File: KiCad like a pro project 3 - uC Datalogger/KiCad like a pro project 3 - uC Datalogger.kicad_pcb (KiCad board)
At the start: 2 copper layers, 29 parts, among them J1 Conn_01x04_Male, J2 Conn_01x09_Male, J3 Conn_01x04_Male, J4 Conn_02x03_Odd_Even, U1 24LC1025, U2 24LC1025, U3 DS1337S+, U4 ATMEGA328P_VQFNVQFN, Y1 32.768 KHz, Y2 16 MHz

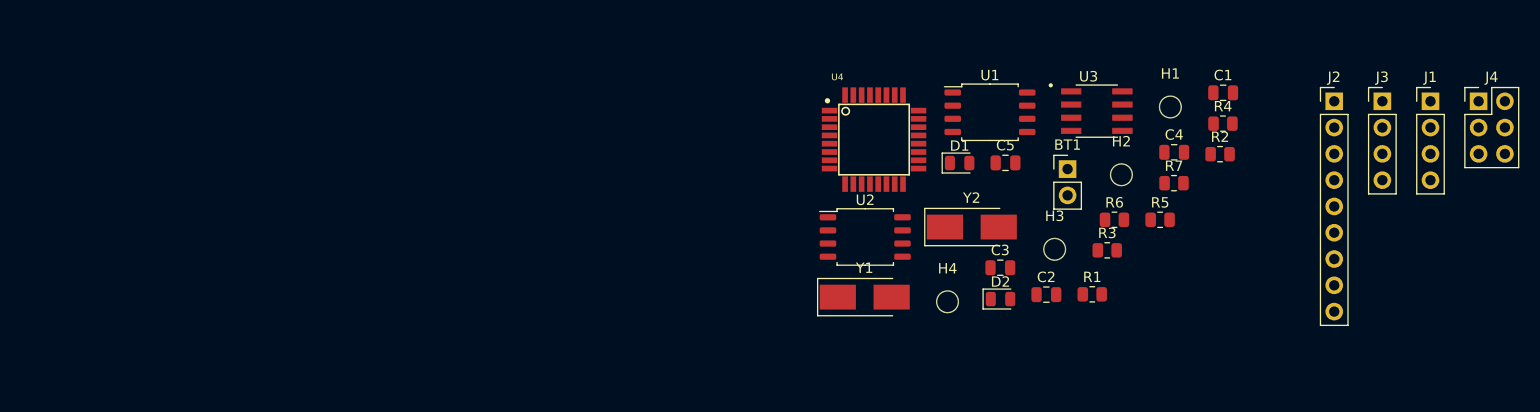
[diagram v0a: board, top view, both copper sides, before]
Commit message: completed placement of foodprints
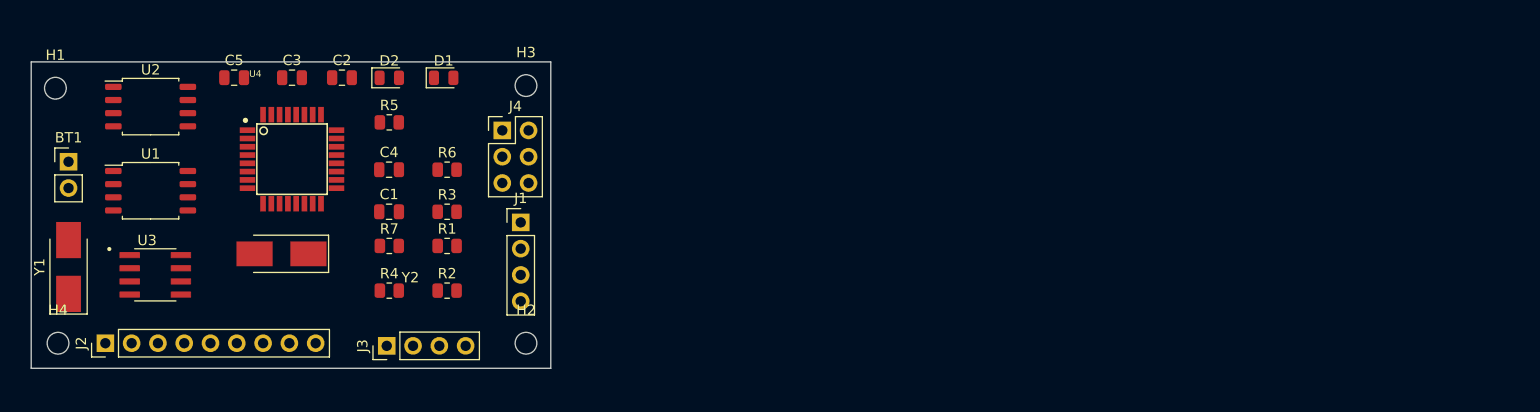
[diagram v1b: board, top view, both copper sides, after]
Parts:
- moved J2 121.0 mm to (54.9, 114.8), turned to 90 degrees
- moved H1 107.7 mm to (50.0, 90.2)
- moved J3 99.0 mm to (82.1, 115.1), turned to 90 degrees
- moved BT1 96.5 mm to (51.3, 97.3)
- moved J4 94.4 mm to (93.2, 94.2)
- moved U3 92.3 mm to (59.7, 108.2)
- moved J1 88.7 mm to (95.0, 103.1)
- moved H4 86.0 mm to (50.3, 114.8)
- moved R4 82.1 mm to (82.3, 109.7)
- moved U1 81.4 mm to (59.2, 100.1)
- moved C1 81.4 mm to (82.3, 102.1)
- moved Y1 77.0 mm to (51.3, 107.4), turned to 90 degrees
- moved R7 76.1 mm to (82.3, 105.4)
- moved C4 75.9 mm to (82.3, 98.0)
- moved R2 75.8 mm to (87.9, 109.7)
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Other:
- board outline added: 50.2 x 29.6 mm

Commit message: Started wiring
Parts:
- moved U3 0.56 mm to (59.1, 108.2)
- moved U1 0.31 mm to (58.9, 100.1)
- moved U2 0.31 mm to (58.9, 91.9)
- turned C1 to 180 degrees
- turned R4 to 180 degrees
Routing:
- net /Vcc: track 0.00 -> 127.1 mm, vias 0 -> 2
- net /SCL: track 0.00 -> 79.0 mm, vias 0 -> 4
- net Net-(BT1-Pad1): track 0.00 -> 52.9 mm, vias 0 -> 2
- net Net-(R2-Pad2): track 0.00 -> 50.3 mm
- net /TX: track 0.00 -> 43.2 mm, vias 0 -> 1
- net GND: track 0.00 -> 38.7 mm, vias 0 -> 3
- net /D2: track 0.00 -> 37.2 mm
- net /RX: track 0.00 -> 35.8 mm, vias 0 -> 1
- net Net-(R4-Pad2): track 0.00 -> 32.1 mm, vias 0 -> 2
- net /SDA: track 0.00 -> 28.7 mm, vias 0 -> 3
- net /D3: track 0.00 -> 27.7 mm
- net /MOSI: track 0.00 -> 26.9 mm, vias 0 -> 1
- net /MISO: track 0.00 -> 25.7 mm
- net /D4: track 0.00 -> 24.7 mm
- net /RESET: track 0.00 -> 22.8 mm, vias 0 -> 2
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- added copper zone on F.Cu, net GND

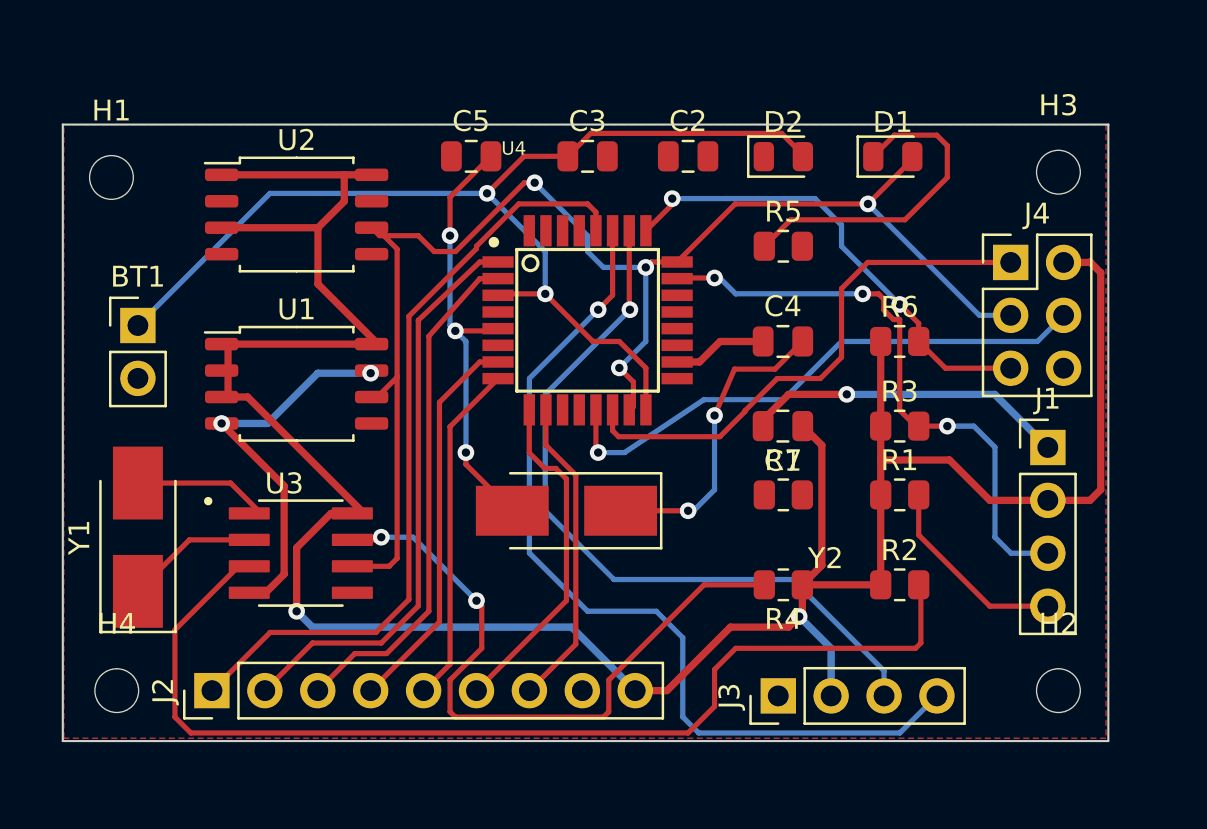
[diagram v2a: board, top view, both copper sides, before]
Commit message: Removed wires, redrawn pcb outline
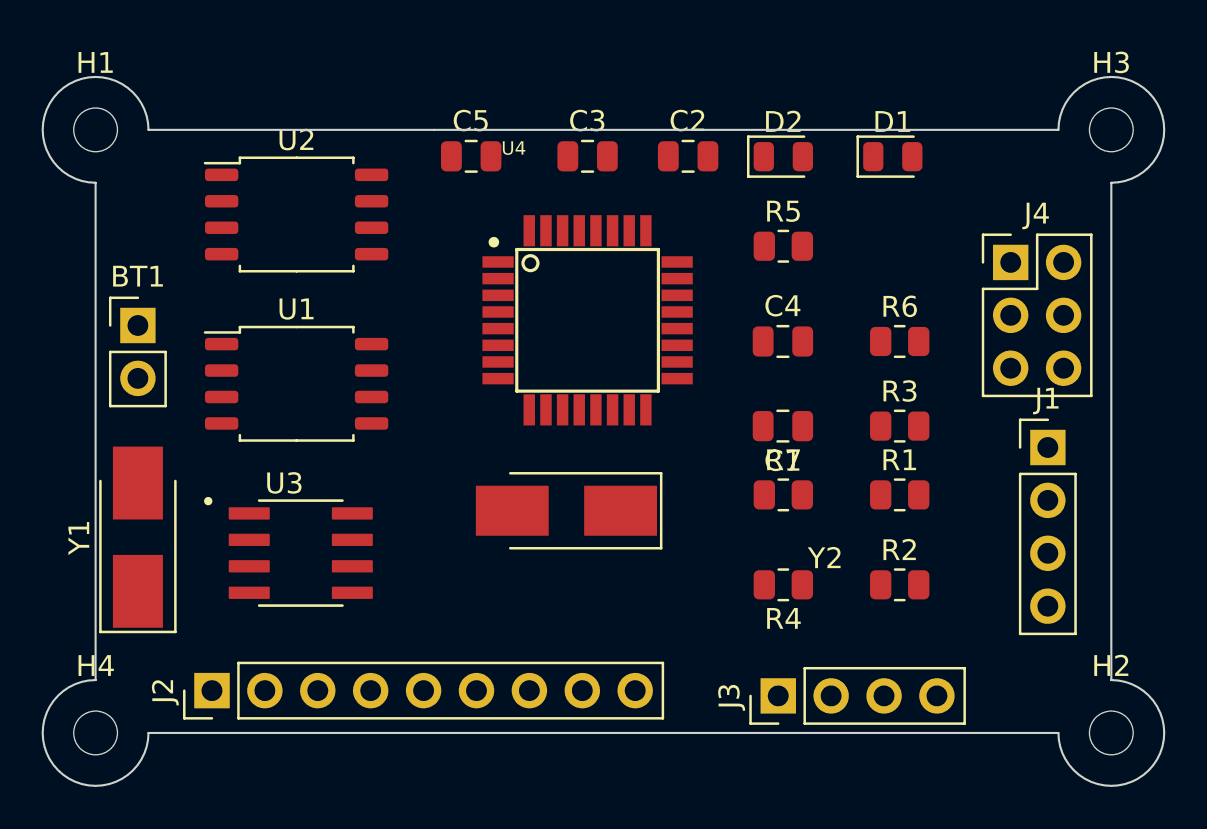
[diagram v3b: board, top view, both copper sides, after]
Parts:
- moved H2 3.25 mm to (98.0, 116.8)
- moved H3 3.25 mm to (98.0, 87.9)
- moved H1 2.41 mm to (49.3, 87.9)
- moved H4 2.27 mm to (49.3, 116.8)
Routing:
- net /Vcc: track 127.1 -> 0.00 mm, vias 2 -> 0
- net /SCL: track 79.0 -> 0.00 mm, vias 4 -> 0
- net Net-(BT1-Pad1): track 52.9 -> 0.00 mm, vias 2 -> 0
- net Net-(R2-Pad2): track 50.3 -> 0.00 mm
- net /TX: track 43.2 -> 0.00 mm, vias 1 -> 0
- net GND: track 38.7 -> 0.00 mm, vias 3 -> 0
- net /D2: track 37.2 -> 0.00 mm
- net /RX: track 35.8 -> 0.00 mm, vias 1 -> 0
- net Net-(R4-Pad2): track 32.1 -> 0.00 mm, vias 2 -> 0
- net /SDA: track 28.7 -> 0.00 mm, vias 3 -> 0
- net /D3: track 27.7 -> 0.00 mm
- net /MOSI: track 26.9 -> 0.00 mm, vias 1 -> 0
- net /MISO: track 25.7 -> 0.00 mm
- net /D4: track 24.7 -> 0.00 mm
- net /RESET: track 22.8 -> 0.00 mm, vias 2 -> 0
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- removed copper zone on F.Cu, net GND
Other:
- board size 50.2 x 29.6 mm -> 53.8 x 34 mm

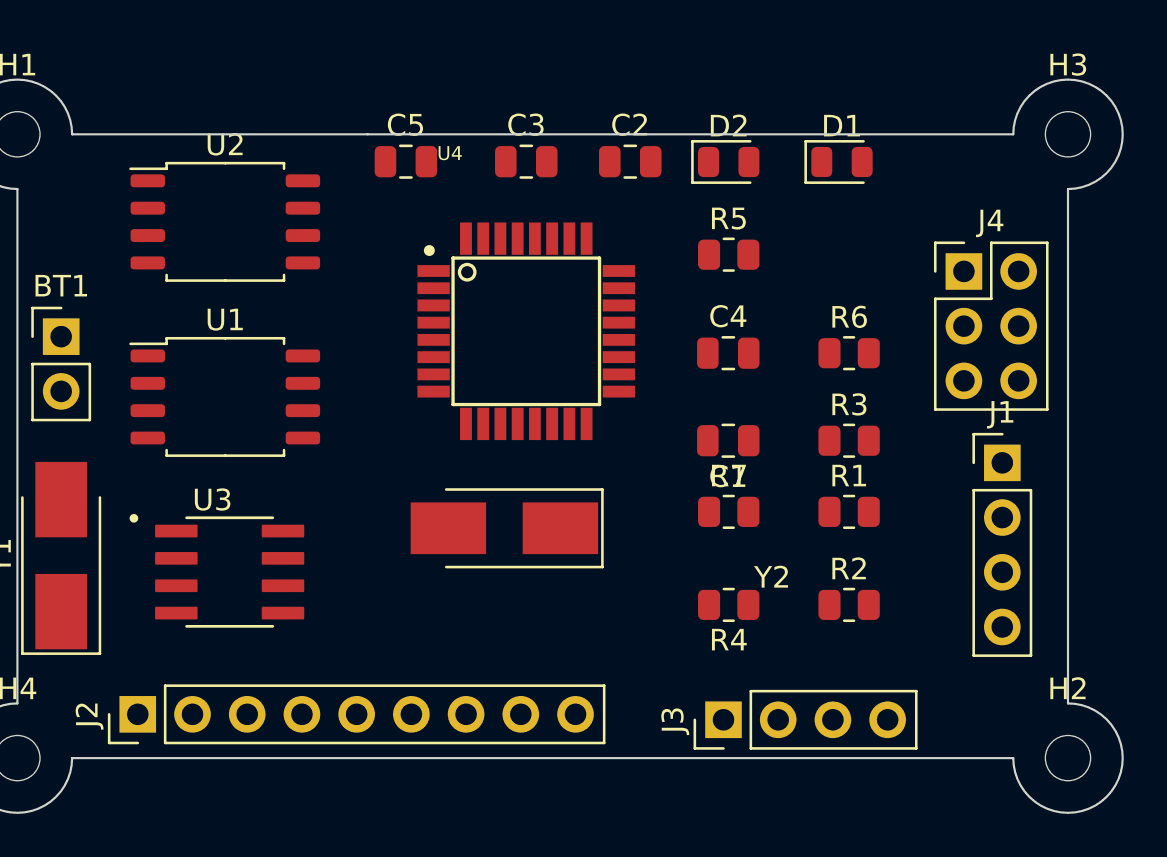
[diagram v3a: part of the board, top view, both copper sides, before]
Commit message: repositioned some components
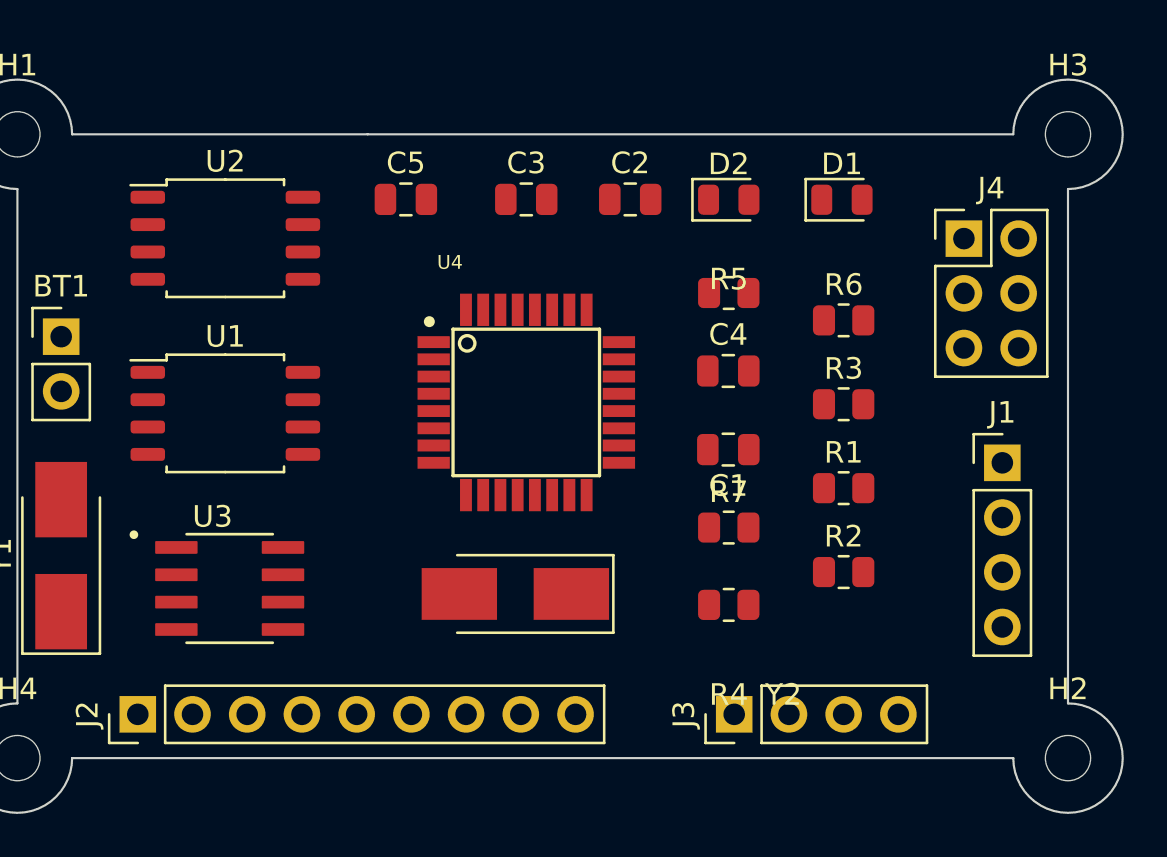
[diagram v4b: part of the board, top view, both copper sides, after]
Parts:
- moved U4 3.30 mm to (72.9, 100.3)
- moved Y2 3.09 mm to (72.4, 109.2)
- moved R5 1.78 mm to (82.3, 95.2)
- moved C2 1.75 mm to (77.7, 90.9)
- moved C3 1.75 mm to (72.9, 90.9)
- moved C5 1.75 mm to (67.3, 90.9)
- moved D1 1.75 mm to (87.6, 90.9)
- moved D2 1.75 mm to (82.3, 90.9)
- moved R3 1.71 mm to (87.6, 100.4)
- moved R2 1.55 mm to (87.6, 108.2)
- moved R6 1.55 mm to (87.6, 96.5)
- moved J4 1.52 mm to (93.2, 92.7)
- moved R1 1.13 mm to (87.6, 104.3)
- moved C4 0.83 mm to (82.3, 98.9)
- moved U1 0.76 mm to (58.9, 100.8)
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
